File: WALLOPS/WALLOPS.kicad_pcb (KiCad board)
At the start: 4 copper layers, 90 x 60 mm, 26 parts, among them J1 JST-PH 1x8 Connector - WALLOP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, Q1 AO3401A, U1 VL53L8CX 0 (Zwicky), U2 VL58L8CX 1 (Aristotle), U3 VL53L8CX 3 (Copernicus), U4 VL53L8CX 2 (Brahe), U5 6DOF IMU (Sisko), U9 TPS62147RGXR

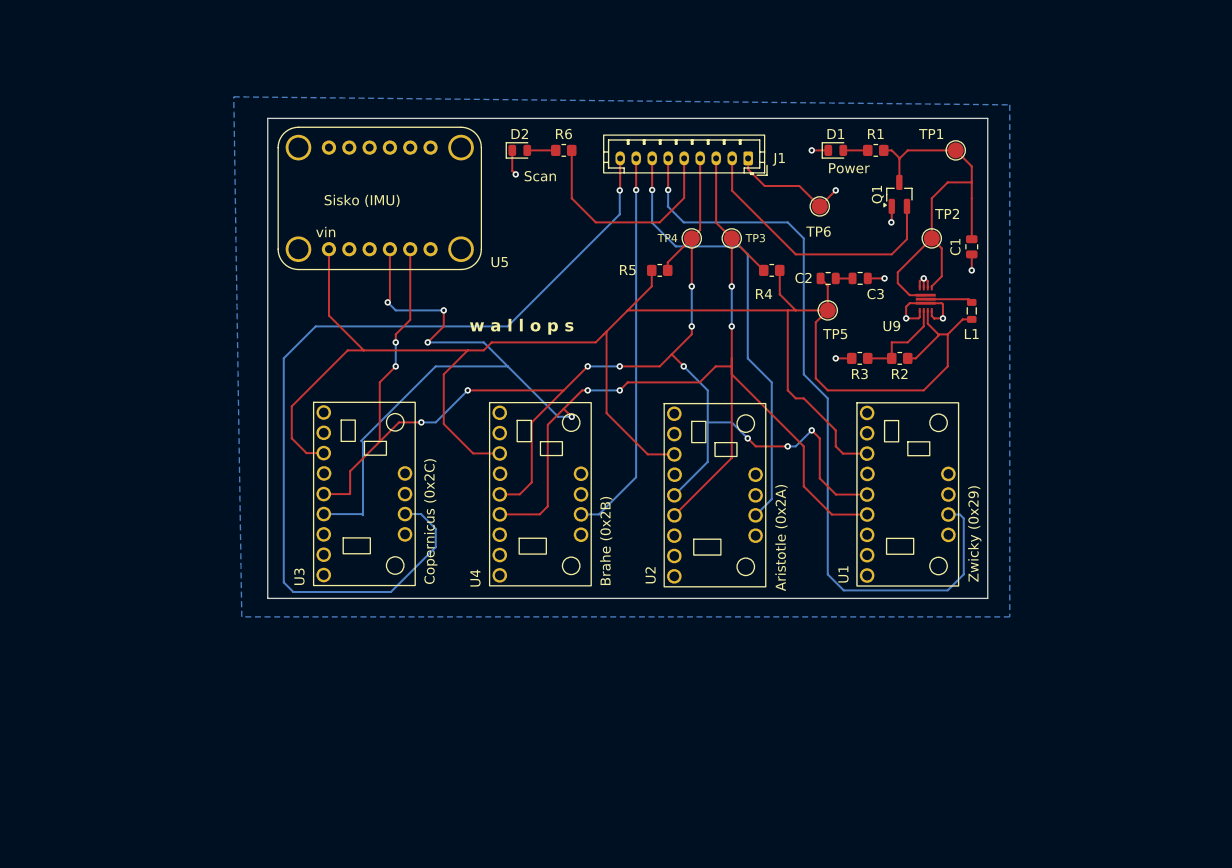
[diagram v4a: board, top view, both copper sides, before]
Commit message: Added updated Wallops PCB + schematic
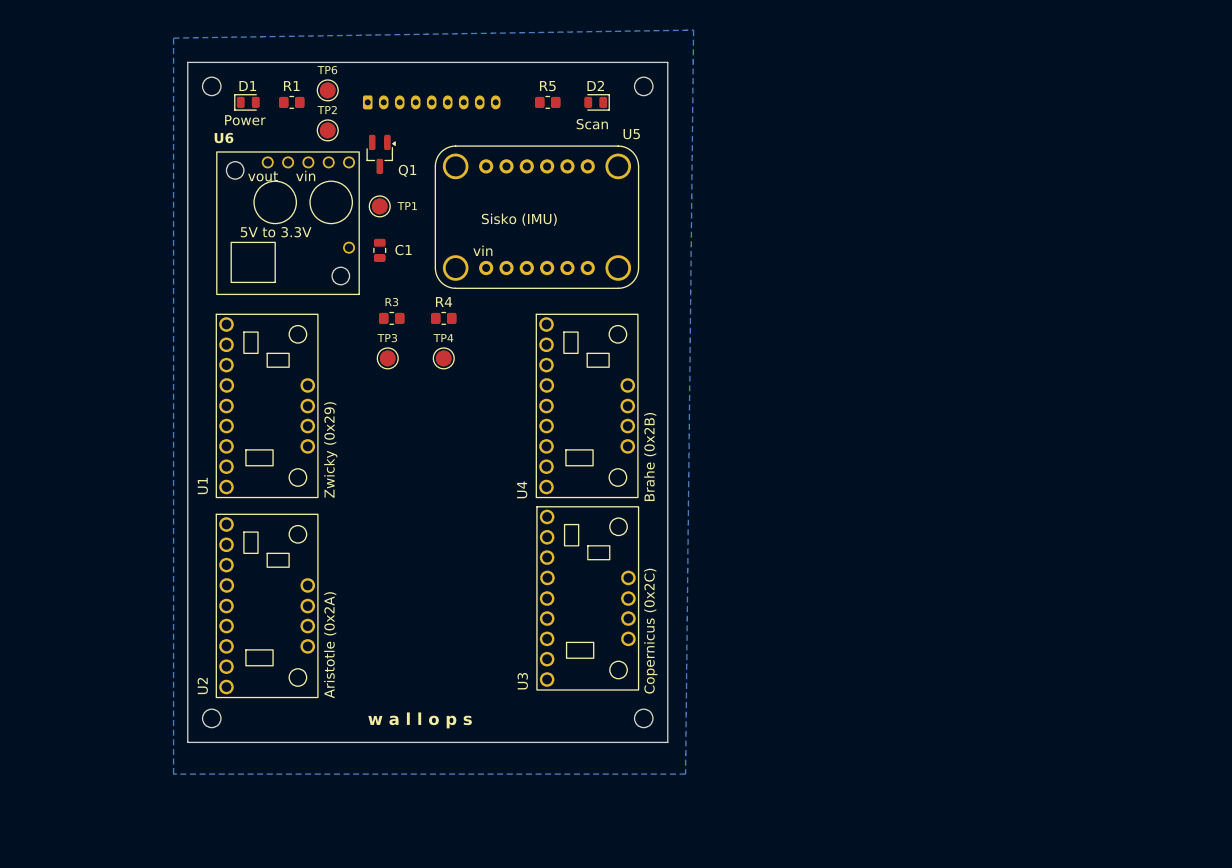
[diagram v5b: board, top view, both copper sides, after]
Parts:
- removed C2, C3: 22µF, Capacitor_SMD:C_0805_2012Metric
- removed L1: 2.2µH, Inductor_SMD:L_0805_2012Metric
- removed R2: 200kΩ, Resistor_SMD:R_0805_2012Metric_Pad1.20x1.40mm_HandSolder
- removed R6: 330Ω, Resistor_SMD:R_0805_2012Metric_Pad1.20x1.40mm_HandSolder
- removed TP5: 3.3VOUT, TestPoint:TestPoint_Pad_D2.0mm
- removed U9: TPS62147RGXR, RockSat:RGX0011A
- added U6: 5V to 3.3V Converter, RockSat:D24V22F3, F.Cu at (82.5, 44.0)
- J1: moved to B.Cu
- R3: value 620kΩ -> 2.2kΩ
- R5: value 2.2kΩ -> 330Ω
- TP1, TP2, TP3, TP4, TP6: footprint TestPoint:TestPoint_Pad_D2.0mm -> RockSat:TestPoint_Pad_D2.0mm_With_Tolerance
- moved U1 80.8 mm to (79.9, 65.9)
- moved TP2 76.7 mm to (87.5, 31.5)
- moved C1 74.0 mm to (94.0, 46.5)
- moved D1 73.7 mm to (77.6, 28.0)
- moved R1 73.2 mm to (83.0, 28.0), turned to 180 degrees
- moved TP1 72.3 mm to (94.0, 41.0)
- moved Q1 65.1 mm to (94.0, 34.5), turned to -90 degrees
- moved TP6 63.2 mm to (87.5, 26.5)
- moved R3 58.7 mm to (95.5, 55.0), turned to 0 degrees
- moved U2 57.7 mm to (79.9, 90.9)
- moved J1 48.1 mm to (92.5, 28.0), turned to 0 degrees
- moved TP3 45.5 mm to (95.0, 60.0)
- moved R4 41.4 mm to (102.0, 55.0)
- moved TP4 34.4 mm to (102.0, 60.0)
- moved U3 30.8 mm to (120.0, 90.0)
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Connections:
- R3 pad 1: Net-(U9-FB) -> /SCL
- R3 pad 2: GND -> /3.3VOUT
- R4 pad 1: /SCL -> /3.3VOUT
- R4 pad 2: /3.3VOUT -> /SDA
- R5 pad 1: /3.3VOUT -> /SCAN_LED
- R5 pad 2: /SDA -> Net-(D2-A)
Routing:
- net /3.3VOUT: track 221.0 -> 0.00 mm
- net /SCL: track 203.6 -> 0.00 mm, vias 8 -> 0
- net /SDA: track 175.4 -> 0.00 mm, vias 12 -> 0
- net /LPn_3: track 113.2 -> 0.00 mm, vias 1 -> 0
- net /LPn_0: track 95.8 -> 0.00 mm, vias 1 -> 0
- net /5Vin: track 88.5 -> 0.00 mm
- net /LPn_1: track 56.4 -> 0.00 mm, vias 1 -> 0
- net /LPn_2: track 48.7 -> 0.00 mm, vias 1 -> 0
- net GND: track 45.6 -> 0.00 mm, vias 10 -> 0
- net /SCAN_LED: track 27.5 -> 0.00 mm
- net Net-(U9-FB): track 11.8 -> 0.00 mm
- net Net-(U9-SW): track 5.92 -> 0.00 mm
- net Net-(D2-A): track 3.56 -> 0.00 mm
- net Net-(D1-A): track 3.06 -> 0.00 mm
- net Net-(C2-Pad2): track 2.10 -> 0.00 mm
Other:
- board size 90 x 60 mm -> 60 x 85 mm
- board text added: "5V to 3.3V"
- board text added: "vout"

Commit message: Added updated WALLOPS PCB
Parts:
- removed TP2: 5V3.3_Test, RockSat:TestPoint_Pad_D2.0mm_With_Tolerance
- C1: value 10µF -> 33µF
- moved C1 19.8 mm to (79.2, 33.3), turned to 0 degrees
- moved TP1 13.5 mm to (84.0, 32.0)
- moved R3 13.3 mm to (94.0, 41.8), turned to -90 degrees
- moved Q1 9.18 mm to (87.0, 28.5)
- moved R4 8.60 mm to (97.3, 47.8), turned to 90 degrees
- moved TP6 7.51 mm to (92.5, 32.1)
- moved TP4 4.17 mm to (98.4, 62.1)
- moved R1 3.16 mm to (80.0, 29.0), turned to 0 degrees
- moved D1 2.75 mm to (75.0, 29.0)
- moved TP3 2.64 mm to (93.7, 62.3)
- moved U5 1.75 mm to (113.7, 44.1)
- moved U6 1.75 mm to (82.6, 45.8)
- moved U1 0.76 mm to (80.0, 66.7)
- moved U2 0.76 mm to (80.0, 91.7)
- moved U3 0.76 mm to (120.1, 90.8)
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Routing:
- net /SCL: track 0.00 -> 188.9 mm, vias 0 -> 6
- net /SDA: track 0.00 -> 184.5 mm, vias 0 -> 1
- net /3.3VOUT: track 0.00 -> 170.6 mm, vias 0 -> 4
- net /LPn_1: track 0.00 -> 155.1 mm, vias 0 -> 4
- net /LPn_3: track 0.00 -> 87.9 mm
- net /LPn_2: track 0.00 -> 61.9 mm
- net /LPn_0: track 0.00 -> 48.5 mm, vias 0 -> 2
- net /5Vin: track 0.00 -> 35.5 mm
- net /SCAN_LED: track 0.00 -> 19.4 mm
- net GND: track 0.00 -> 15.5 mm, vias 0 -> 5
- net Net-(D2-A): track 0.00 -> 4.06 mm
- net Net-(D1-A): track 0.00 -> 3.06 mm
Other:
- board size 60 x 85 mm -> 60 x 90 mm
- board text added: "Aristotle"
- board text added: "Brahe"
- board text added: "Copernicus"
- board text added: "Zwicky"
- board text removed: "Aristotle (0x2A)"
- board text removed: "Brahe (0x2B)"
- board text removed: "Copernicus (0x2C)"
- board text removed: "Zwicky (0x29)"
